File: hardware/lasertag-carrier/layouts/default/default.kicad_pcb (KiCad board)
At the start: 2 copper layers, 37 parts, among them J0 Power in 2P, J1 S3-Matrix L, J10 LS in, J11 LS out, J12 Ext button, J13 Touch hdr, J2 S3-Matrix R, J3 MAX98357A, J4 Speaker, J5 microSD, J6 IR RX, J7 IR LED, J8 WS2812 out, J9 OLED I2C, Q1 2N2222A, SW1 SW_PUSH_6mm, U1 74AHCT125

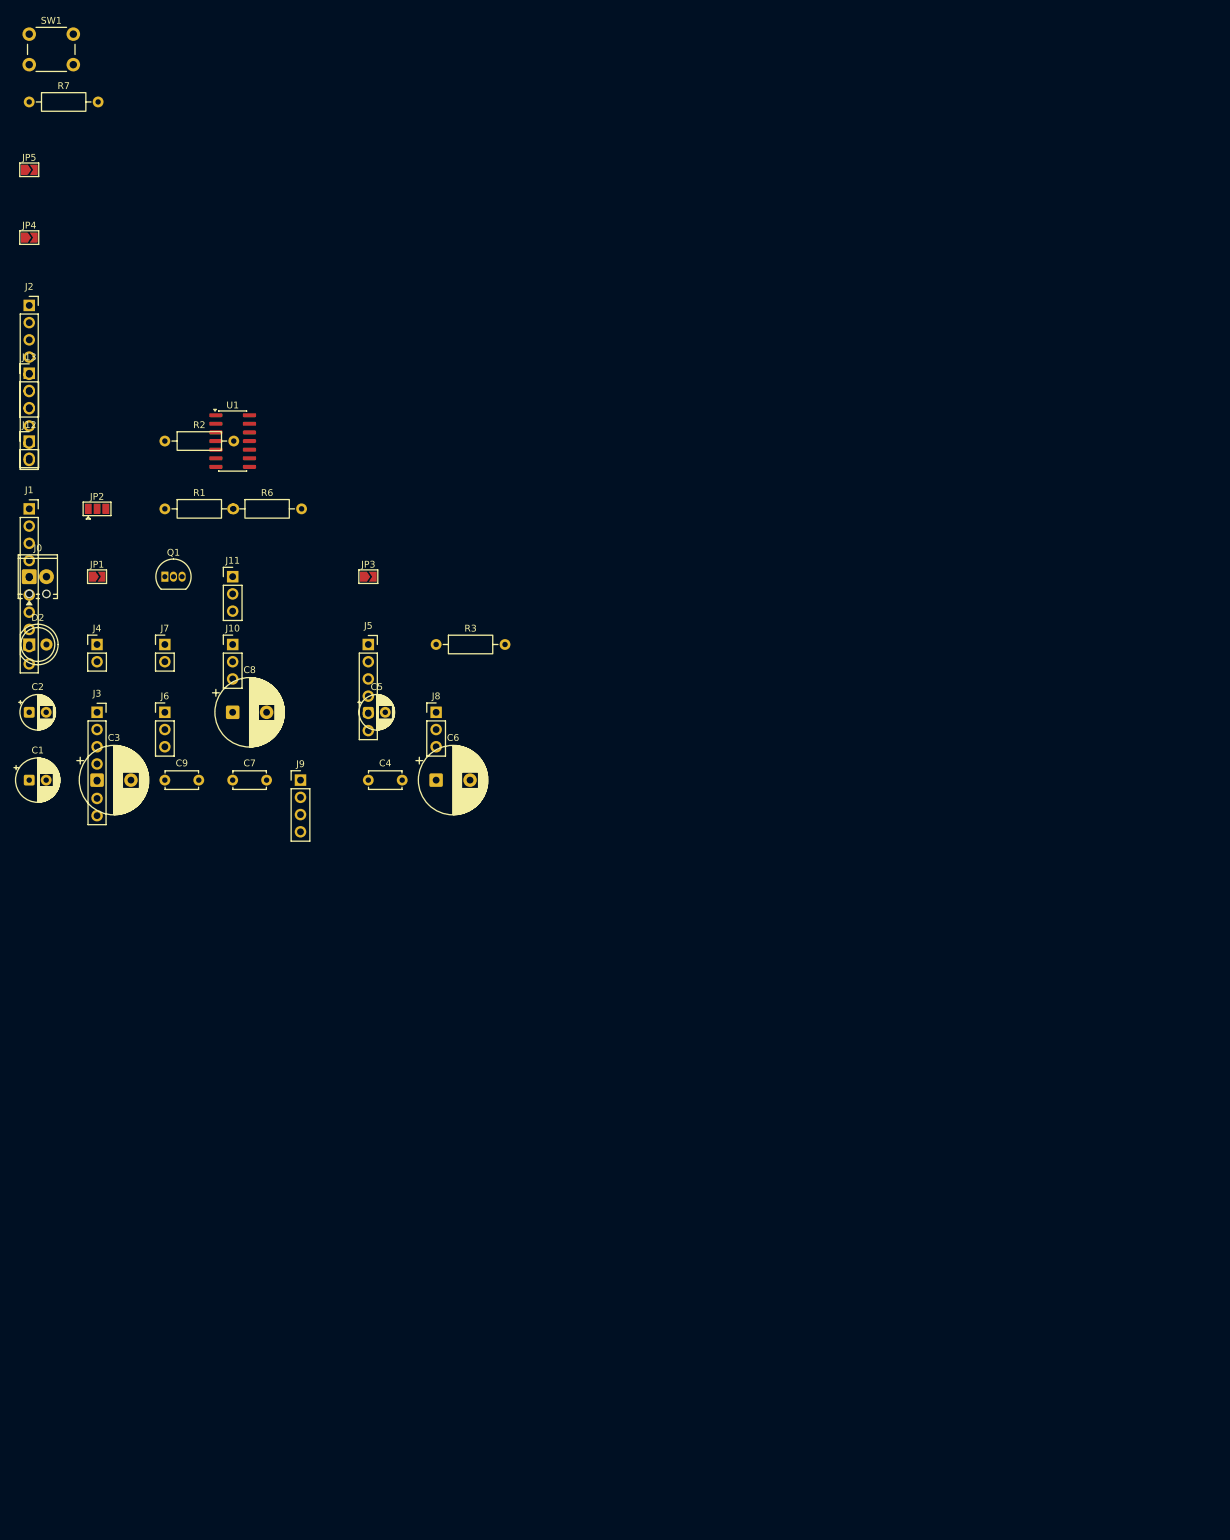
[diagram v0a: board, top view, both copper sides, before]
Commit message: Place carrier footprints on a 75x50mm board outline
Everything was sitting on atopile's default 10mm scatter grid with no board
outline, which made parts hard to select and produced 164 DRC errors.

- add a 75 x 50 mm Edge.Cuts outline
- centre the ESP32-S3-Matrix sockets J1/J2 on the board, rows exactly
  22.86 mm (9 x 2.54) apart so the module seats
- shelf-pack the other 35 footprints into the free space around the module,
  sized from each footprint's real pad+graphics bounding box with a 1.2 mm gap

Verified: 37/37 inside the outline, zero overlapping bounding boxes, and DRC
errors 164 -> 0. Remaining DRC output is 84 unconnected items (the unrouted
ratsnest) plus silkscreen-overlap warnings, both expected pre-routing.

Co-Authored-By: Claude Opus 4.8 <noreply@anthropic.com>
Claude-Session: https://claude.ai/code/session_01TutNLcDSScdeeVSbjpyg8j
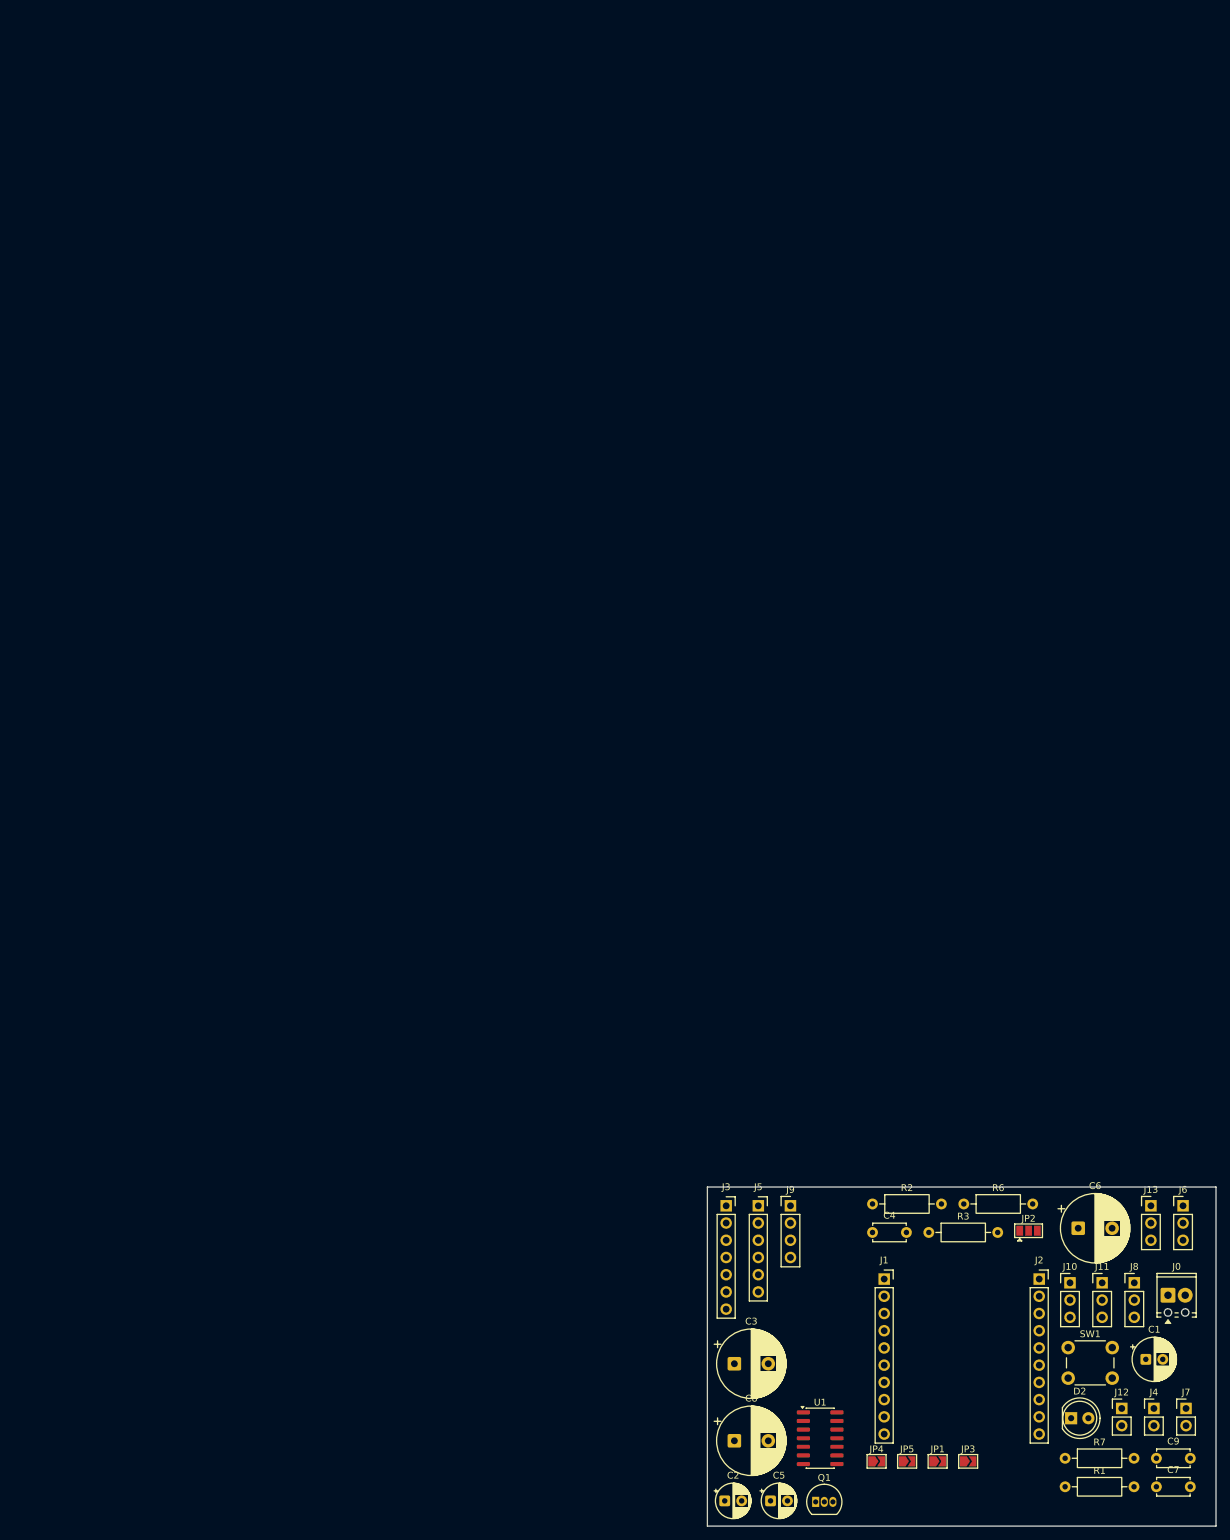
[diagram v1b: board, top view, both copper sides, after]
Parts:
- moved R7 251.7 mm to (152.8, 100.0)
- moved SW1 246.9 mm to (153.2, 83.7)
- moved JP5 230.3 mm to (129.4, 100.5)
- moved JP4 219.5 mm to (125.0, 100.5)
- moved J12 215.2 mm to (161.1, 92.7)
- moved J2 206.9 mm to (148.9, 73.6)
- moved J13 206.0 mm to (165.4, 62.8)
- moved J0 198.6 mm to (167.9, 76.0)
- moved R1 196.0 mm to (152.8, 104.2)
- moved J4 192.3 mm to (165.8, 92.7)
- moved D2 191.4 mm to (153.6, 94.1)
- moved J7 188.1 mm to (170.6, 92.7)
- moved C1 185.5 mm to (164.7, 85.4)
- moved JP1 179.9 mm to (133.9, 100.5)
- moved C9 177.1 mm to (166.2, 100.0)
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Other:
- board outline added: 75 x 50 mm
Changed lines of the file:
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@@
     (footprint "Capacitor_THT:CP_Radial_D6.3mm_P2.50mm"
         (layer "F.Cu")
-        (at 0 0 0)
+        (at 164.650 85.410)
         (property "Reference" "C1"
             (at 1.25 -4.4 0)
@@
     (footprint "Capacitor_THT:CP_Radial_D5.0mm_P2.50mm"
         (layer "F.Cu")
-        (at 0 -10 0)
+        (at 102.555 106.280)
         (property "Reference" "C2"
             (at 1.25 -3.75 0)
@@
     (footprint "LED_THT:LED_D5.0mm"
         (layer "F.Cu")
-        (at 0 -20 0)
+        (at 153.640 94.090)
         (property "Reference" "D2"
             (at 1.27 -3.96 0)
@@
     (footprint "TerminalBlock_Phoenix:TerminalBlock_Phoenix_MPT-0,5-2-2.54_1x02_P2.54mm_Horizontal"
         (layer "F.Cu")
-        (at 0 -30 0)
+        (at 167.920 75.960)
         (property "Reference" "J0"
             (at 1.27 -4.22 0)
@@
     (footprint "Connector_PinSocket_2.54mm:PinSocket_1x10_P2.54mm_Vertical"
         (layer "F.Cu")
-        (at 0 -40 0)
+        (at 126.070 73.570)
         (property "Reference" "J1"
             (at 0 -2.77 0)
@@
     (footprint "Connector_PinHeader_2.54mm:PinHeader_1x02_P2.54mm_Vertical"
         (layer "F.Cu")
-        (at 0 -50 0)
+        (at 161.100 92.650)
         (property "Reference" "J12"
             (at 0 -2.38 0)
@@
     (footprint "Connector_PinHeader_2.54mm:PinHeader_1x03_P2.54mm_Vertical"
         (layer "F.Cu")
-        (at 0 -60 0)
+        (at 165.400 62.770)
         (property "Reference" "J13"
             (at 0 -2.38 0)
@@
     (footprint "Connector_PinSocket_2.54mm:PinSocket_1x10_P2.54mm_Vertical"
         (layer "F.Cu")
-        (at 0 -70 0)
+        (at 148.930 73.570)
         (property "Reference" "J2"
             (at 0 -2.77 0)
@@
     (footprint "LocalJumper:SolderJumper-2"
         (layer "F.Cu")
-        (at 0 -80 0)
+        (at 124.950 100.450)
         (property "Reference" "JP4"
             (at 0 -1.8 0)
@@
     (footprint "LocalJumper:SolderJumper-2"
         (layer "F.Cu")
-        (at 0 -90 0)
+        (at 129.450 100.450)
         (property "Reference" "JP5"
             (at 0 -1.8 0)
@@
     (footprint "Resistor_THT:R_Axial_DIN0207_L6.3mm_D2.5mm_P10.16mm_Horizontal"
         (layer "F.Cu")
-        (at 0 -100 0)
+        (at 152.750 100.000)
         (property "Reference" "R7"
             (at 5.08 -2.37 0)
@@
     (footprint "Button_Switch_THT:SW_PUSH_6mm_H5mm"
         (layer "F.Cu")
-        (at 0 -110 0)
+        (at 153.200 83.680)
         (property "Reference" "SW1"
             (at 3.25 -2 0)
@@
     (footprint "Capacitor_THT:CP_Radial_D10.0mm_P5.00mm"
         (layer "F.Cu")
-        (at 10 0 0)
+        (at 103.980 86.060)
         (property "Reference" "C3"
             (at 2.5 -6.25 0)
@@
     (footprint "Connector_PinSocket_2.54mm:PinSocket_1x07_P2.54mm_Vertical"
         (layer "F.Cu")
-        (at 10 -10 0)
+        (at 102.770 62.770)
         (property "Reference" "J3"
             (at 0 -2.77 0)
@@
     (footprint "Connector_PinHeader_2.54mm:PinHeader_1x02_P2.54mm_Vertical"
         (layer "F.Cu")
-        (at 10 -20 0)
+        (at 165.840 92.650)
         (property "Reference" "J4"
             (at 0 -2.38 0)
@@
     (footprint "LocalJumper:SolderJumper-2"
         (layer "F.Cu")
-        (at 10 -30 0)
+        (at 133.950 100.450)
         (property "Reference" "JP1"
             (at 0 -1.8 0)
@@
     (footprint "LocalJumper:SolderJumper-3"
         (layer "F.Cu")
-        (at 10 -40 0)
+        (at 147.360 66.450)
         (property "Reference" "JP2"
             (at 0 -1.8 0)
@@
     (footprint "Capacitor_THT:C_Disc_D4.7mm_W2.5mm_P5.00mm"
         (layer "F.Cu")
-        (at 20 0 0)
+        (at 166.210 100.000)
         (property "Reference" "C9"
             (at 2.5 -2.5 0)
@@
     (footprint "Connector_PinHeader_2.54mm:PinHeader_1x03_P2.54mm_Vertical"
         (layer "F.Cu")
-        (at 20 -10 0)
+        (at 170.140 62.770)
         (property "Reference" "J6"
             (at 0 -2.38 0)
@@
     (footprint "Connector_PinHeader_2.54mm:PinHeader_1x02_P2.54mm_Vertical"
         (layer "F.Cu")
-        (at 20 -20 0)
+        (at 170.580 92.650)
         (property "Reference" "J7"
             (at 0 -2.38 0)
@@
     (footprint "Package_TO_SOT_THT:TO-92_Inline"
         (layer "F.Cu")
-        (at 20 -30 0)
+        (at 115.970 106.430)
         (property "Reference" "Q1"
             (at 1.27 -3.56 0)
@@
     (footprint "Resistor_THT:R_Axial_DIN0207_L6.3mm_D2.5mm_P10.16mm_Horizontal"
         (layer "F.Cu")
-        (at 20 -40 0)
+        (at 152.750 104.200)
         (property "Reference" "R1"
             (at 5.08 -2.37 0)
@@
     (footprint "Resistor_THT:R_Axial_DIN0207_L6.3mm_D2.5mm_P10.16mm_Horizontal"
         (layer "F.Cu")
-        (at 20 -50 0)
+        (at 124.350 62.500)
         (property "Reference" "R2"
             (at 5.08 -2.37 0)
@@
     (footprint "Capacitor_THT:C_Disc_D4.7mm_W2.5mm_P5.00mm"
         (layer "F.Cu")
-        (at 30 0 0)
+        (at 166.210 104.200)
         (property "Reference" "C7"
             (at 2.5 -2.5 0)
@@
     (footprint "Capacitor_THT:CP_Radial_D10.0mm_P5.00mm"
         (layer "F.Cu")
-        (at 30 -10 0)
+        (at 103.980 97.420)
         (property "Reference" "C8"
             (at 2.5 -6.25 0)
@@
     (footprint "Connector_PinHeader_2.54mm:PinHeader_1x03_P2.54mm_Vertical"
         (layer "F.Cu")
-        (at 30 -20 0)
+        (at 153.470 74.130)
         (property "Reference" "J10"
             (at 0 -2.38 0)
@@
     (footprint "Connector_PinHeader_2.54mm:PinHeader_1x03_P2.54mm_Vertical"
         (layer "F.Cu")
-        (at 30 -30 0)
+        (at 158.210 74.130)
         (property "Reference" "J11"
             (at 0 -2.38 0)
@@
     (footprint "Resistor_THT:R_Axial_DIN0207_L6.3mm_D2.5mm_P10.16mm_Horizontal"
         (layer "F.Cu")
-        (at 30 -40 0)
+        (at 137.810 62.500)
         (property "Reference" "R6"
             (at 5.08 -2.37 0)
@@
     (footprint "Package_SO:SOIC-14_3.9x8.7mm_P1.27mm"
         (layer "F.Cu")
-        (at 30 -50 0)
+        (at 116.630 97.040)
         (property "Reference" "U1"
             (at 0 -5.28 0)
@@
     (footprint "Connector_PinHeader_2.54mm:PinHeader_1x04_P2.54mm_Vertical"
         (layer "F.Cu")
-        (at 40 0 0)
+        (at 112.250 62.770)
         (property "Reference" "J9"
             (at 0 -2.38 0)
@@
     (footprint "Capacitor_THT:C_Disc_D4.7mm_W2.5mm_P5.00mm"
         (layer "F.Cu")
-        (at 50 0 0)
+        (at 124.350 66.700)
         (property "Reference" "C4"
             (at 2.5 -2.5 0)
@@
     (footprint "Capacitor_THT:CP_Radial_D5.0mm_P2.50mm"
         (layer "F.Cu")
-        (at 50 -10 0)
+        (at 109.310 106.280)
         (property "Reference" "C5"
             (at 1.25 -3.75 0)
@@
     (footprint "Connector_PinSocket_2.54mm:PinSocket_1x06_P2.54mm_Vertical"
         (layer "F.Cu")
-        (at 50 -20 0)
+        (at 107.510 62.770)
         (property "Reference" "J5"
             (at 0 -2.77 0)
@@
     (footprint "LocalJumper:SolderJumper-2"
         (layer "F.Cu")
-        (at 50 -30 0)
+        (at 138.450 100.450)
         (property "Reference" "JP3"
             (at 0 -1.8 0)
@@
     (footprint "Capacitor_THT:CP_Radial_D10.0mm_P5.00mm"
         (layer "F.Cu")
-        (at 60 0 0)
+        (at 154.680 66.080)
         (property "Reference" "C6"
             (at 2.5 -6.25 0)
@@
     (footprint "Connector_PinHeader_2.54mm:PinHeader_1x03_P2.54mm_Vertical"
         (layer "F.Cu")
-        (at 60 -10 0)
+        (at 162.950 74.130)
         (property "Reference" "J8"
             (at 0 -2.38 0)
@@
     (footprint "Resistor_THT:R_Axial_DIN0207_L6.3mm_D2.5mm_P10.16mm_Horizontal"
         (layer "F.Cu")
-        (at 60 -20 0)
+        (at 132.650 66.700)
         (property "Reference" "R3"
             (at 5.08 -2.37 0)
@@
         )
     )
+	(gr_line
+		(start 100.0 60.0)
+		(end 175.0 60.0)
+		(stroke
+			(width 0.1)
+			(type default)
+		)
+		(layer "Edge.Cuts")
+	)
+	(gr_line
+		(start 175.0 60.0)
+		(end 175.0 110.0)
+		(stroke
+			(width 0.1)
+			(type default)
+		)
+		(layer "Edge.Cuts")
+	)
+	(gr_line
+		(start 175.0 110.0)
+		(end 100.0 110.0)
+		(stroke
+			(width 0.1)
+			(type default)
+		)
+		(layer "Edge.Cuts")
+	)
+	(gr_line
+		(start 100.0 110.0)
+		(end 100.0 60.0)
+		(stroke
+			(width 0.1)
+			(type default)
+		)
+		(layer "Edge.Cuts")
+	)
 )
